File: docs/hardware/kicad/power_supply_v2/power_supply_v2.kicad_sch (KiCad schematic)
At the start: 99 parts, among them J1 Barrel_Jack, J2 LOAD 3V3, J3 LOAD 5V, J4 LOAD Vvar, Q1 MMBT3904LT1G, Q2 AO3401A, SW2 Rotary_Encoder_3_Pin, U1 TPS54302, U14 SHT31-DIS, U15 SHT31-DIS, U2 MCP1700T-3302E/TT, U3 MCP1700T-3302E/TT, U4 TPS54302, U5 MCP1700T-5002E/TT, U6 TPS54302, U7 TPS54302, U8 TPS22917DBV, U9 TPS22917DBV

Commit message: updated schematic for LC filters and added voltage injection to other… (#4)
* updated schematic for LC filters and added voltage injection to other bucks

* rework buck resistor divider values + add fb injection to 3V3 and 5V rail bucks

* remove redundant switches for variable rail

* remove datasheets for components no longer used in rev A3

---------

Co-authored-by: chris <chris@laptop.malecki.com>
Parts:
- removed C11, C18, C9: 1μF, symbol Library:C_Small
- removed D2: B340A-13-F, digikey-footprints:DO-214AC, symbol Library:B340A-13-F
- removed Q1: MMBT3904LT1G, digikey-footprints:SOT-23-3, symbol Library:MMBT3904LT1G
- removed Q2: AO3401A, digikey-footprints:SOT-23-3, symbol Library:AO3401A
- removed R12: 10mR, symbol Library:R_Small_US
- removed R21, R23: 1kR, symbol Library:R_Small_US
- removed R22, R24: 10kR, symbol Library:R_Small_US
- removed S1: ~, symbol Library:Button_Array_4
- removed U3: MCP1700T-3302E/TT, digikey-footprints:SOT-23-3, symbol Library:MCP1700T-3302E_TT
- added C10, C19, C32, C33: 10μF, symbol Library:C_Small
- added L2, L4, L7: 1μH, symbol Library:L_Iron
- added R17: 470R, symbol Library:R_Small_US
- added R4: 68kR, symbol Library:R_Small_US
- added R9: 47kR, symbol Library:R_Small_US
- added S2: SW_Button_4, symbol Library:Button_Array_4
- R16: renamed from R15; value 3kR92 -> 3kR3
- R18: renamed from R16; value 25kR5 -> 22kR
- R3: value 19kR2 -> 22kR
- R8: renamed from R7; value 12kR1 -> 15kR
- S1: renamed from SW2; value Rotary_Encoder_3_Pin -> Rotary_Encoder_3
- U2: value MCP1700T-3302E/TT -> MCP1700T
- U5: value MCP1700T-5002E/TT -> MCP1700T
- renumbered C12 to C11, C13 to C12, C14 to C13, C15 to C14, C16 to C15, C17 to C16, C19 to C17, C20 to C18, C21 to C20, C22 to C21, C23 to C22, C24 to C23, C25 to C24, C26 to C25, C27 to C26, C28 to C27, C29 to C28, C30 to C29, C31 to C30, C32 to C31, C33 to C34, C34 to C35, C35 to C36, C36 to C37, C37 to C38, C38 to C39, C39 to C40, C40 to C41, C41 to C42, C10 to C9, L2 to L3, L3 to L5, L4 to L6, R8 to R10, R9 to R11, R10 to R12, R11 to R13, R13 to R14, R14 to R15, R17 to R19, R18 to R20, R19 to R21, R20 to R22, R25 to R27, R4 to R5, R5 to R6, R6 to R7, U14 to U16, U15 to U17
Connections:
- net +3V3B: now also C10.1, L2.2
- net +3V7: now also L2.1
- net +5V5: now also L4.1
- net +5VA: now also C18.1, U5.2 (OUT)
- net +5VB: now also C19.1, L4.2; no longer C18.1, U5.2 (OUT)
- net +V_{VAR}: now also L7.1
- net BUCK_12V_EN: now also R11.1; no longer R11.2
- net GNDREF: now also C10.2, C19.2, C32.2, C33.2, R17.2, S2.5 (GND); no longer R16.2
- net INA_V_{VAR}_IN+: now also C32.1, C33.1, L7.2
- net Microcontroller/BTN_3V3B_PB7: now also S2.1 (B1)
- net Microcontroller/BTN_5VB_PC13: now also S2.2 (B2)
- net Microcontroller/BTN_DSP_PC15: now also S2.4 (B4)
- net Microcontroller/BTN_VVAR_PC14: now also S2.3 (B3)
- net Microcontroller/BUCK_VVAR_EN_PC5: now also R14.1; no longer R14.2
- net at C7.2, R2.2, R3.1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: now also R4.1
- net at C16.2, R7.2, R8.1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: now also R9.1
- net at U7.5 (EN): now also R14.2; no longer R14.1
- net at U6.5 (EN): now also R11.2; no longer R11.1
- new net: R16.2, R17.1
- new net DAC_3V7_PA6: R4.2
- new net DAC_5V5_PA5: R9.2
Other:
- sheet Current_Sensors ports: added none; removed INA_12V_IN+, INA_12V_IN-, INA_12V_OUT_PB13
- sheet Microcontroller ports: added DAC_3V7_PA6, DAC_5V5_PA5; removed INA_12V_OUT_PB13, NPN_V_{VAR}_PA0
- note added: "MCU & peripherals power"
- note added: "V_{out} = 0.596 * (1 + R15 / (R16 + R17) + R15 / R18) - V_{DAC} * (R15 / R18) V_{DAC} = 0 to 3V3 R15 / (R16 + R17) = 26R53 R15 / R18 = 4R55 When V_{DAC} = 0, V_{OUT} = 19V12 When V_{DAC} = 3V3, V_{OUT} = 4V1"
- note added: "V_{out} = 0.596 * (1 + R2 / R3 + R2 / R4) - V_{DAC} * (R2 / R4) V_{DAC} = 0 to 3V3 R2 / R3 = 4R54 R2 / R4 = 1R47 When V_{DAC} = 0, V_{OUT} = 4V18 When V_{DAC} = 3V3, V_{OUT} = -0V67 Will only be used to out to compensate for voltage drop across protection diodes"
- note added: "V_{out} = 0.596 * (1 + R7 / R8 + R7 / R9) - V_{DAC} * (R7 / R9) V_{DAC} = 0 to 3V3 R7 / R8 = 2R13 R7 / R9 = 6R67 When V_{DAC} = 0, V_{OUT} = 5V84 When V_{DAC} = 3V3, V_{OUT} = -1V19 Will only be used to out to compensate for voltage drop across protection diodes"
- note added: "fan power"
- note added: "voltage buffer for fan PWM and LED data"
- note removed: "V_{f(MAX)}=0V5"
- note removed: "V_{out} = 0.596 * (1 + R2 / R1 + R2 / R3) - V_{DAC} * (R2 / R3) V_{DAC} = 0 to 3V3 R2 / R3 = ~3.92 R2 / R1 = ~25.51 When V_{DAC} = 0, V_{OUT} = 18.14V When V_{DAC} = 3V3, V_{OUT} = 5.2V"
- moved on the sheet: C1, C17, C18, C42, C8, C9, D1, D7, D8, DS3, DS4, J1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

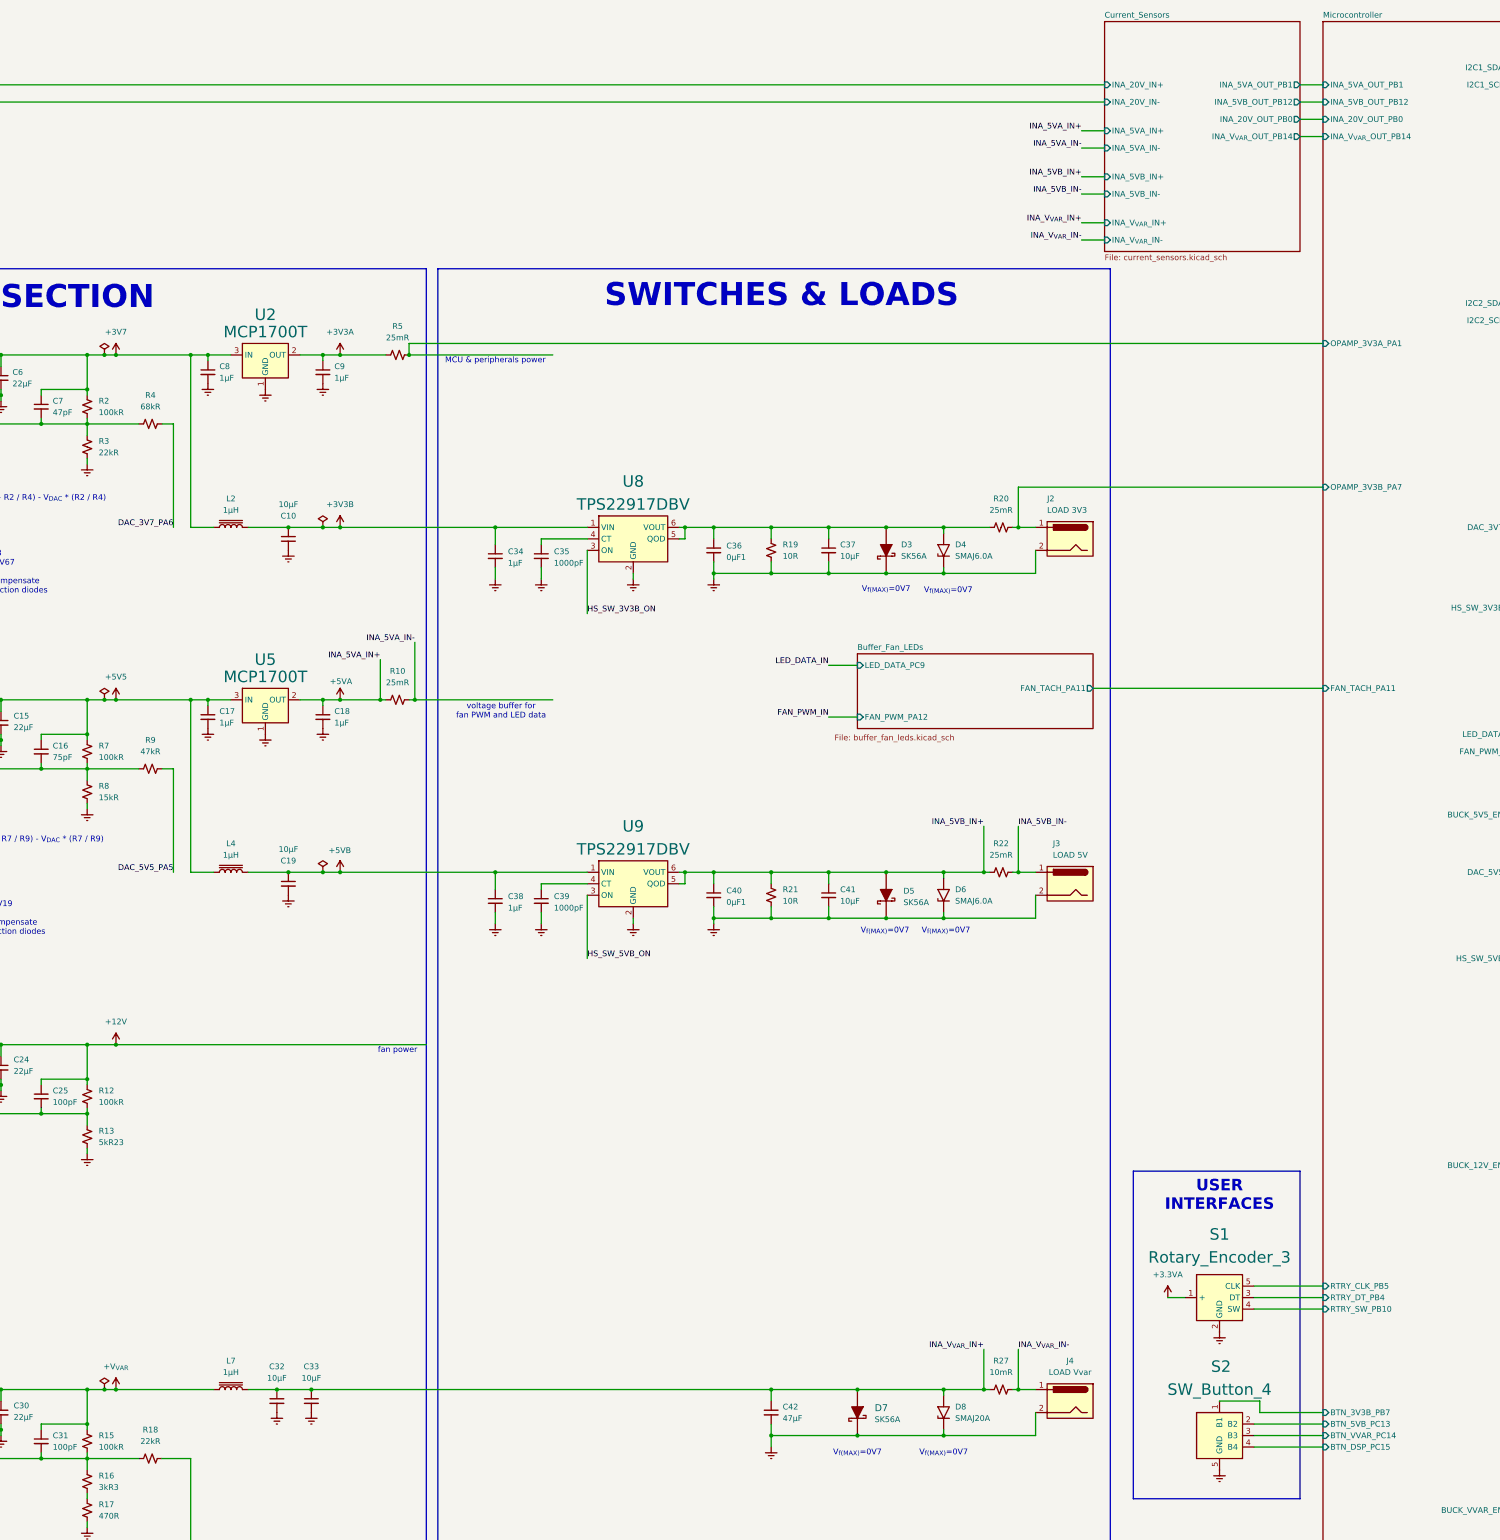
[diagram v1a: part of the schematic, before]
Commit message: update schematic to fix power rail node and update resistors to reflect series to reach target dividers
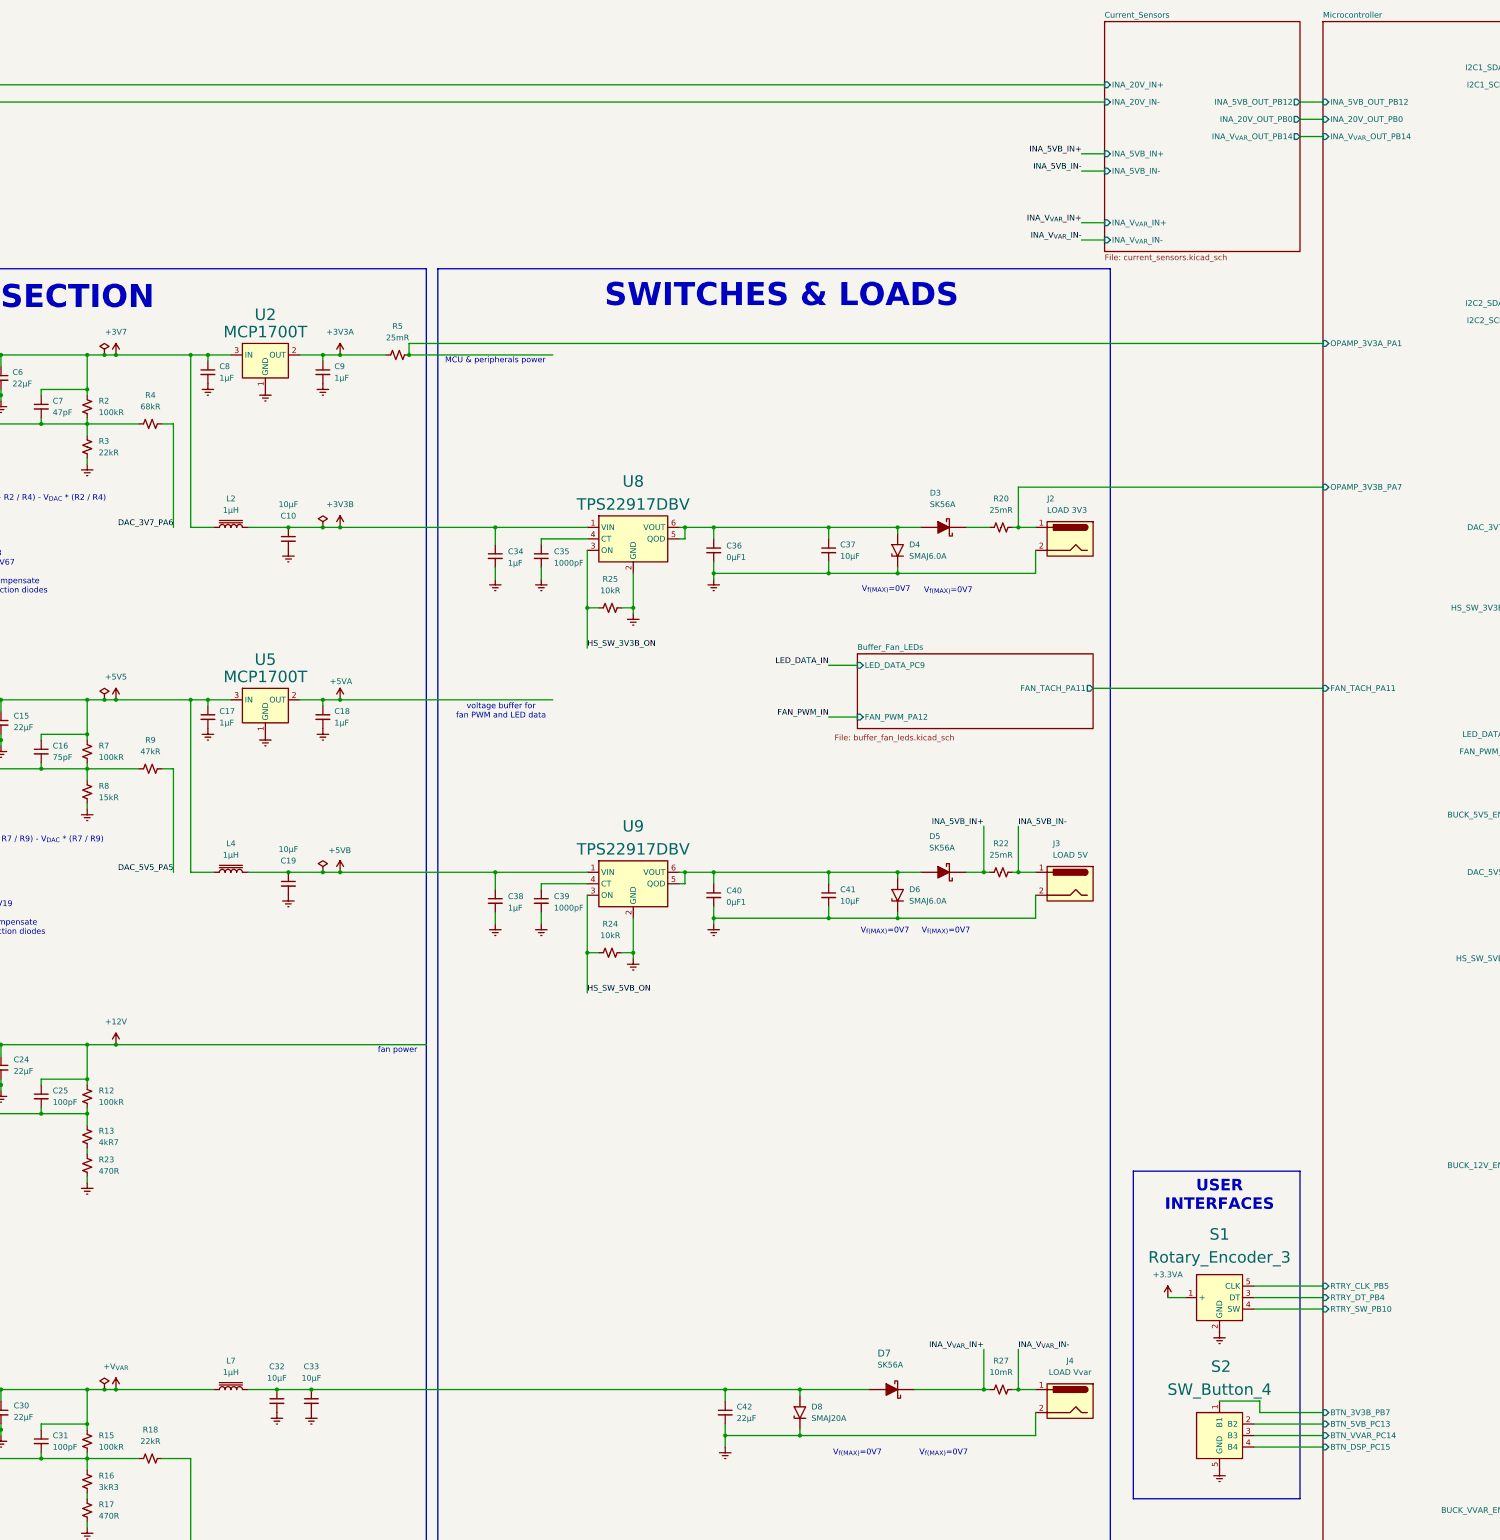
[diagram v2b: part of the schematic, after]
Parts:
- removed R10: 25mR, symbol Library:R_Small_US
- removed R19, R21: 10R, symbol Library:R_Small_US
- added R23: 470R, symbol Library:R_Small_US
- added R24, R25: 10kR, symbol Library:R_Small_US
- C42: value 47μF -> 22μF
- R13: value 5kR23 -> 4kR7
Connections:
- net GNDREF: now also R23.2, R24.2, R25.2; no longer D3.K, D5.K, D7.K, R13.2
- net HS_SW_3V3B_ON: now also R25.1
- net HS_SW_5VB_ON: now also R24.1
- net INA_5VB_IN+: now also D5.K; no longer C40.1, C41.1, D5.A, D6.2 (A2), U9.5 (QOD), U9.6 (VOUT)
- net INA_V_{VAR}_IN+: now also D7.K; no longer C32.1, C33.1, C42.1, D7.A, D8.2 (A2), L7.2
- net at C36.1, C37.1, D3.A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: no longer R20.1
- new net: D3.K, R20.1
- new net: C32.1, C33.1, C42.1, D7.A, D8.2 (A2), L7.2
- new net: C40.1, C41.1, D5.A, D6.2 (A2), U9.5 (QOD), U9.6 (VOUT)
- new net: R13.2, R23.1
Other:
- sheet Current_Sensors ports: added none; removed INA_5VA_IN+, INA_5VA_IN-, INA_5VA_OUT_PB1
- sheet Microcontroller ports: added none; removed INA_5VA_OUT_PB1
- moved on the sheet: C42, D3, D4, D5, D6, D7, D8

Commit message: rev 4A for schematic to reflect changes from assembling
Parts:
- added C44: 0μF1, symbol Library:C_Small
- added D2: WS2812, LED_SMD:LED_WS2812B-2020_PLCC4_2.0x2.0mm, symbol Library:WS2812B-2020
- added M1: Fan_4pin, symbol Library:Fan_4pin
- added R10, R19, R26: 10kR, symbol Library:R_Small_US
- added R21: 470R, symbol Library:R_Small_US
- added U11: NUCLEO-G474RE, NUCLEO-G474RE:MODULE_NUCLEO-G474RE, symbol Library:NUCLEO-G474RE
- added U12, U18: INA180A3, Package_TO_SOT_SMD:SOT-23-5, symbol Library:INA180A3
- added U19: INA180A1, Package_TO_SOT_SMD:SOT-23-5, symbol Library:INA180A3
- added U3: SN74AHCT125N, digikey-footprints:DIP-14_W3mm, symbol Library:SN74AHCT125N
- DS3, DS4: value OLED_96in_64x128_I2C -> OLED_64x128_I2C
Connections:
- net +12V: now also M1.2 (+)
- net +20V: now also U12.4 (-)
- net +3.3VA: now also R26.1
- net +3V3A: now also U11.CN7_16 (+3V3), U12.5 (V+), U18.5 (V+), U19.5 (V+)
- net +5VA: now also C44.1, D2.4 (VDD), U3.14 (VCC)
- net DAC_3V7_PA6: now also U11.CN10_13 (PA6)
- net DAC_5V5_PA5: now also U11.CN10_11 (PA5)
- net GNDREF: now also C44.2, D2.2 (VSS), M1.1 (-), R10.2, R19.2, U11.CN7_8 (GND_CN7_8), U12.2 (GND), U18.2 (GND), U19.2 (GND), U3.10 (3~{OE}), U3.12 (4A), U3.13 (4~{OE}), U3.7 (GND), U3.9 (3A)
- net INA_5VB_IN+: now also U19.3 (+)
- net INA_5VB_IN-: now also U19.4 (-)
- net INA_V_{VAR}_IN+: now also U18.3 (+)
- net INA_V_{VAR}_IN-: now also U18.4 (-)
- net BUCK_12V_EN renamed BUCK_12V_EN_PC6
- net BUCK_12V_EN_PC6: now also U11.CN10_4 (PC6)
- net BUCK_5V5_EN renamed BUCK_5V5_EN_PC8
- net BUCK_5V5_EN_PC8: now also U11.CN10_2 (PC8)
- net Current_Sensors/INA_20V_IN+ renamed INA_20V_IN+
- net INA_20V_IN+: now also U12.3 (+)
- net HS_SW_3V3B_ON renamed HS_SW_3V3B_PC2
- net HS_SW_3V3B_PC2: now also U11.CN7_35 (PC2)
- net HS_SW_5VB_ON renamed HS_SW_5VB_PC3
- net HS_SW_5VB_PC3: now also U11.CN7_37 (PC3)
- net Microcontroller/BTN_3V3B_PB7 renamed BTN_3V3B_PB7
- net BTN_3V3B_PB7: now also U11.CN7_21 (PB7)
- net Microcontroller/BTN_5VB_PC13 renamed BTN_5VB_PC13
- net BTN_5VB_PC13: now also U11.CN7_23 (PC13)
- net Microcontroller/BTN_DSP_PC15 renamed BTN_DSP_PC15
- net BTN_DSP_PC15: now also U11.CN7_27 (PC15)
- net Microcontroller/BTN_VVAR_PC14 renamed BTN_V_{VAR}_PC14
- net BTN_V_{VAR}_PC14: now also U11.CN7_25 (PC14)
- net Microcontroller/BUCK_VVAR_EN_PC5 renamed BUCK_V_{VAR}_EN_PC5
- net BUCK_V_{VAR}_EN_PC5: now also U11.CN10_6 (PC5)
- net Microcontroller/DAC_V_{VAR}_PA4 renamed DAC_V_{VAR}_PA4
- net DAC_V_{VAR}_PA4: now also U11.CN7_32 (PA4)
- net Microcontroller/I2C1_SCL_PB8 renamed I2C1_SCL_PB8
- net I2C1_SCL_PB8: now also U16.4 (SCL), U11.CN10_3 (PB8); no longer DS4.4 (SCL)
- net Microcontroller/I2C1_SDA_PB9 renamed I2C1_SDA_PB9
- net I2C1_SDA_PB9: now also U16.1 (SDA), U11.CN10_5 (PB9); no longer DS4.3 (SDA)
- net Microcontroller/I2C2_SCL_PA9 renamed I2C2_SCL_PA9
- net I2C2_SCL_PA9: now also DS4.4 (SCL), U11.CN10_21 (PA9); no longer U16.4 (SCL)
- net Microcontroller/I2C2_SDA_PA8 renamed I2C2_SDA_PA8
- net I2C2_SDA_PA8: now also DS4.3 (SDA), U11.CN10_23 (PA8); no longer U16.1 (SDA)
- net Microcontroller/OPAMP_3V3A_PA1 renamed OPAMP_3V3A_PA1
- net OPAMP_3V3A_PA1: now also U11.CN7_30 (PA1)
- net Microcontroller/OPAMP_3V3B_PA7 renamed OPAMP_3V3B_PA7
- net OPAMP_3V3B_PA7: now also U11.CN10_15 (PA7)
- net Microcontroller/RTRY_CLK_PB5 renamed RTRY_CLK_PB5
- net RTRY_CLK_PB5: now also U11.CN10_29 (PB5)
- net Microcontroller/RTRY_DT_PB4 renamed RTRY_DT_PB4
- net RTRY_DT_PB4: now also U11.CN10_27 (PB4)
- net Microcontroller/RTRY_SW_PB10 renamed RTRY_SW_PB10
- net RTRY_SW_PB10: now also U11.CN10_25 (PB10)
- new net: D2.3 (DIN), R21.1
- new net: R21.2, U3.3 (1Y)
- new net: M1.4 (PWM), U3.6 (2Y)
- new net: R19.1, U3.1 (1~{OE})
- new net: R10.1, U3.4 (2~{OE})
- new net FAN_PWM_PA12: U11.CN10_12 (PA12), U3.5 (2A)
- new net FAN_TACH_PA11: M1.3 (Tacho), R26.2, U11.CN10_14 (PA11)
- new net INA_20V_OUT_PB0: U11.CN7_34 (PB0), U12.1
- new net INA_5VB_OUT_PB12: U11.CN10_16 (PB12), U19.1
- new net INA_V_{VAR}_OUT_PB14: U11.CN10_28 (PB14), U18.1
- new net LED_DATA_PC9: U11.CN10_1 (PC9), U3.2 (1A)
- no-connect marks 5 -> 48
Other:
- removed sheet Buffer_Fan_LEDs
- removed sheet Current_Sensors
- removed sheet Microcontroller
- note added: "4x LED series"
- note added: "GND"
- note added: "IN+"
- note added: "IN-"
- note added: "LOADS"
- note added: "MCU"
- note added: "OUT"
- note added: "POWER/BUCKS"
- note added: "Pin assignment is not optimized or based on any physical layout currently."
- note added: "REGULATION"
- note added: "SWITCHES"
- note added: "VS"
- note added: "V_{out} = 0.596 * (1 + R2 / R3 + R2 / R4) - V_{DAC} * (R2 / R4) V_{DAC} = 0 to 3V3 R2 / R3 = 4R54 R2 / R4 = 1R47 When V_{DAC} = 0, V_{OUT} = 4V18 When V_{DAC} = 3V3, V_{OUT} = -0V67"
- note added: "V_{out} = 0.596 * (1 + R7 / R8 + R7 / R9) - V_{DAC} * (R7 / R9) V_{DAC} = 0 to 3V3 R7 / R8 = 2R13 R7 / R9 = 6R67 When V_{DAC} = 0, V_{OUT} = 5V84 When V_{DAC} = 3V3, V_{OUT} = -1V19"
- note removed: "MCU & peripherals power"
- note removed: "POWER SECTION"
- note removed: "SWITCHES & LOADS"
- note removed: "V_{f(MAX)}=0V7"
- note removed: "V_{out} = 0.596 * (1 + R2 / R3 + R2 / R4) - V_{DAC} * (R2 / R4) V_{DAC} = 0 to 3V3 R2 / R3 = 4R54 R2 / R4 = 1R47 When V_{DAC} = 0, V_{OUT} = 4V18 When V_{DAC} = 3V3, V_{OUT} = -0V67 Will only be used to out to compensate for voltage drop across protection diodes"
- note removed: "V_{out} = 0.596 * (1 + R7 / R8 + R7 / R9) - V_{DAC} * (R7 / R9) V_{DAC} = 0 to 3V3 R7 / R8 = 2R13 R7 / R9 = 6R67 When V_{DAC} = 0, V_{OUT} = 5V84 When V_{DAC} = 3V3, V_{OUT} = -1V19 Will only be used to out to compensate for voltage drop across protection diodes"
- note removed: "voltage buffer for fan PWM and LED data"
- moved on the sheet: C1, C10, C11, C12, C13, C14, C15, C16, C17, C18, C19, C2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

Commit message: update schematic and README
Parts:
- renumbered C34 to C11, C35 to C12, C36 to C13, C37 to C14, C11 to C15, C12 to C16, C13 to C17, C14 to C18, C15 to C19, C16 to C20, C17 to C21, C18 to C22, C19 to C23, C44 to C24, C38 to C25, C39 to C26, C40 to C27, C41 to C28, C20 to C29, C21 to C30, C22 to C31, C23 to C32, C24 to C33, C25 to C34, C26 to C35, C27 to C36, C28 to C37, C29 to C38, C30 to C39, C31 to C40, C32 to C41, C33 to C42, C42 to C43, D4 to D2, D2 to D4, D6 to D5, D5 to D6, D8 to D7, D7 to D8, DS3 to DS1, DS4 to DS2, R8 to R10, R9 to R11, R10 to R12, R19 to R13, R21 to R14, R26 to R15, R24 to R16, R22 to R17, R11 to R18, R12 to R19, R13 to R20, R23 to R21, R14 to R22, R15 to R23, R16 to R24, R17 to R25, R18 to R26, R25 to R6, R20 to R7, R6 to R8, R7 to R9, U11 to U10, U12 to U11, U18 to U12, U19 to U13, U16 to U14, U17 to U15, U8 to U3, U3 to U6, U9 to U7, U6 to U8, U7 to U9
